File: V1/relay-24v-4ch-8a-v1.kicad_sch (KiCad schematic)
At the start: 22 parts, among them J1 DG141V-2.54-6P, J2 DB142V-5.08-8P, K1 G5Q-1A4-DC24V, K2 G5Q-1A4-DC24V, K3 G5Q-1A4-DC24V, K4 G5Q-1A4-DC24V

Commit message: Prefab checks
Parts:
- D1, D3, D5, D7: value GREEN -> EMERALD; LCSC Part # C72043 -> C2984266; Mfr Everlight -> Everlight Elec; Mfr PN 19-217/GHC-YR1S2/3T -> 19-213/GHC-XS1T1N/5T; Vendor PN C72043 -> C2984266
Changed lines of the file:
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@@
 			)
 		)
-		(property "Value" "GREEN"
+		(property "Value" "EMERALD"
 			(at 162.56 120.65 90)
 			(effects
@@
 			)
 		)
-		(property "Mfr" "Everlight"
+		(property "Mfr" "Everlight Elec"
 			(at 165.1 120.65 0)
 			(effects
@@
 			)
 		)
-		(property "Mfr PN" "19-217/GHC-YR1S2/3T"
+		(property "Mfr PN" "19-213/GHC-XS1T1N/5T"
 			(at 165.1 120.65 0)
 			(effects
@@
 			)
 		)
-		(property "Vendor PN" "C72043"
+		(property "Vendor PN" "C2984266"
 			(at 165.1 120.65 0)
 			(effects
@@
 			)
 		)
-		(property "LCSC Part #" "C72043"
+		(property "LCSC Part #" "C2984266"
 			(at 162.56 123.19 90)
 			(effects
@@
 			)
 		)
-		(property "Value" "GREEN"
+		(property "Value" "EMERALD"
 			(at 74.93 118.11 90)
 			(effects
@@
 			)
 		)
-		(property "Mfr" "Everlight"
+		(property "Mfr" "Everlight Elec"
 			(at 77.47 118.11 0)
 			(effects
@@
 			)
 		)
-		(property "Mfr PN" "19-217/GHC-YR1S2/3T"
+		(property "Mfr PN" "19-213/GHC-XS1T1N/5T"
 			(at 77.47 118.11 0)
 			(effects
@@
 			)
 		)
-		(property "Vendor PN" "C72043"
+		(property "Vendor PN" "C2984266"
 			(at 77.47 118.11 0)
 			(effects
@@
 			)
 		)
-		(property "LCSC Part #" "C72043"
+		(property "LCSC Part #" "C2984266"
 			(at 74.93 120.65 90)
 			(effects
@@
 			)
 		)
-		(property "Value" "GREEN"
+		(property "Value" "EMERALD"
 			(at 74.93 80.01 90)
 			(effects
@@
 			)
 		)
-		(property "Mfr" "Everlight"
+		(property "Mfr" "Everlight Elec"
 			(at 77.47 80.01 0)
 			(effects
@@
 			)
 		)
-		(property "Mfr PN" "19-217/GHC-YR1S2/3T"
+		(property "Mfr PN" "19-213/GHC-XS1T1N/5T"
 			(at 77.47 80.01 0)
 			(effects
@@
 			)
 		)
-		(property "Vendor PN" "C72043"
+		(property "Vendor PN" "C2984266"
 			(at 77.47 80.01 0)
 			(effects
@@
 			)
 		)
-		(property "LCSC Part #" "C72043"
+		(property "LCSC Part #" "C2984266"
 			(at 74.93 82.55 90)
 			(effects
@@
 			)
 		)
-		(property "Value" "GREEN"
+		(property "Value" "EMERALD"
 			(at 162.56 82.55 90)
 			(effects
@@
 			)
 		)
-		(property "Mfr" "Everlight"
+		(property "Mfr" "Everlight Elec"
 			(at 165.1 82.55 0)
 			(effects
@@
 			)
 		)
-		(property "Mfr PN" "19-217/GHC-YR1S2/3T"
+		(property "Mfr PN" "19-213/GHC-XS1T1N/5T"
 			(at 165.1 82.55 0)
 			(effects
@@
 			)
 		)
-		(property "Vendor PN" "C72043"
+		(property "Vendor PN" "C2984266"
 			(at 165.1 82.55 0)
 			(effects
@@
 			)
 		)
-		(property "LCSC Part #" "C72043"
+		(property "LCSC Part #" "C2984266"
 			(at 162.56 85.09 90)
 			(effects

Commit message: Updated footprints
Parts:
- removed J2: DB142V-5.08-8P, Tales:TerminalBlock_Dibo_DB142V-5.08-8P_1x08_P5.08mm_Vertical, symbol Connector_Generic:Conn_01x08
- added J2, J3: Conn_01x04, Tales:TerminalBlock_Dibo_DB142V-5.08-4P_1x04_P5.08mm_Vertical, symbol Connector_Generic:Conn_01x04
- J1: value DG141V-2.54-6P -> DB141V-2.54-6P; LCSC Part # C2898747 -> C2898748; Mfr DIBO -> DORABO; Vendor PN C2898747 -> C2898748
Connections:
- net at K3.2, RV3.2: now also J3.2 (Pin_2)
- net at K3.3, RV3.1: now also J3.1 (Pin_1)
- net at K4.2, RV4.2: now also J3.4 (Pin_4)
- net at K4.3, RV4.1: now also J3.3 (Pin_3)
- net at K1.2, RV1.2: now also J2.2 (Pin_2)
- net at K1.3, RV1.1: now also J2.1 (Pin_1)
- net at K2.3, RV2.1: now also J2.3 (Pin_3)
- net at K2.2, RV2.2: now also J2.4 (Pin_4)

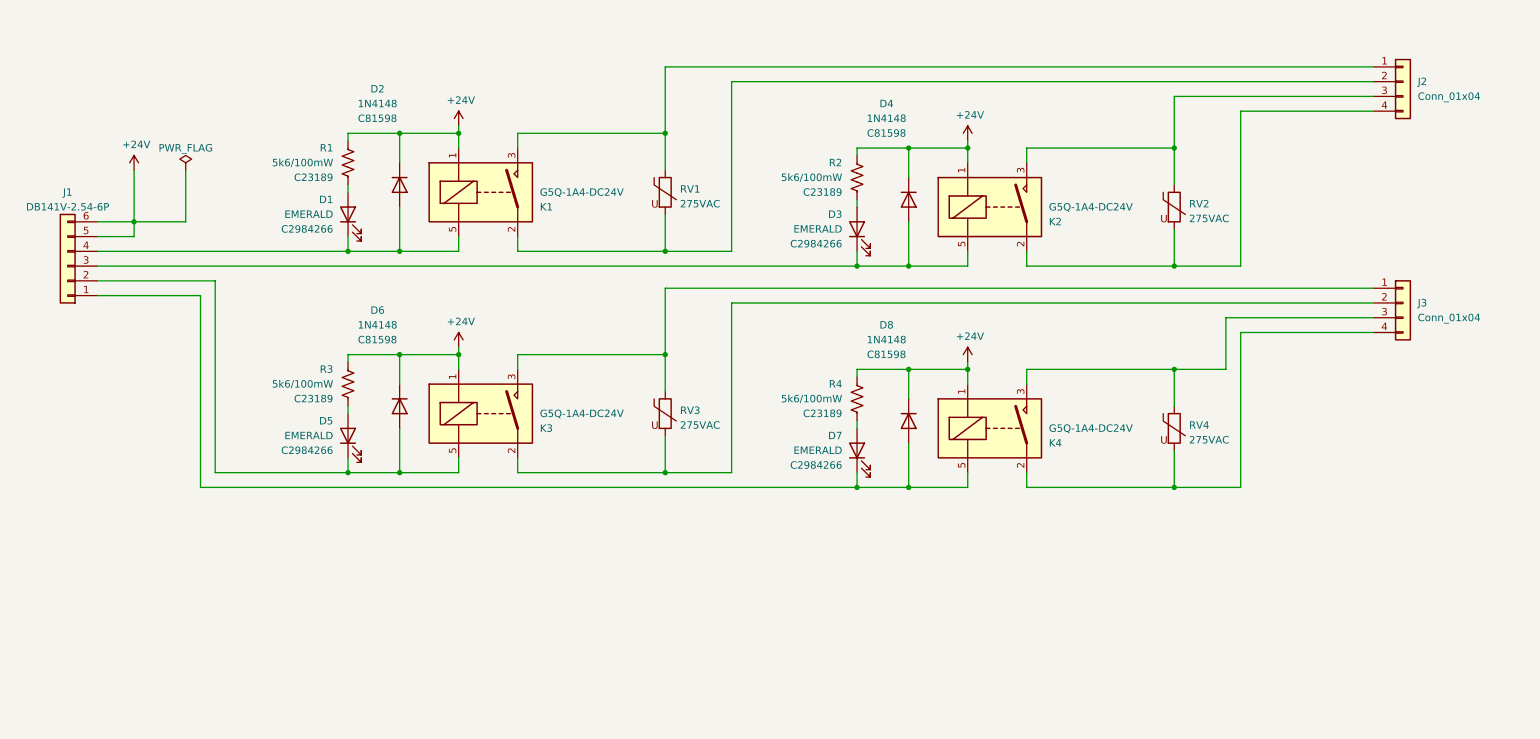
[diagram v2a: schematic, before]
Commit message: Updated connectors
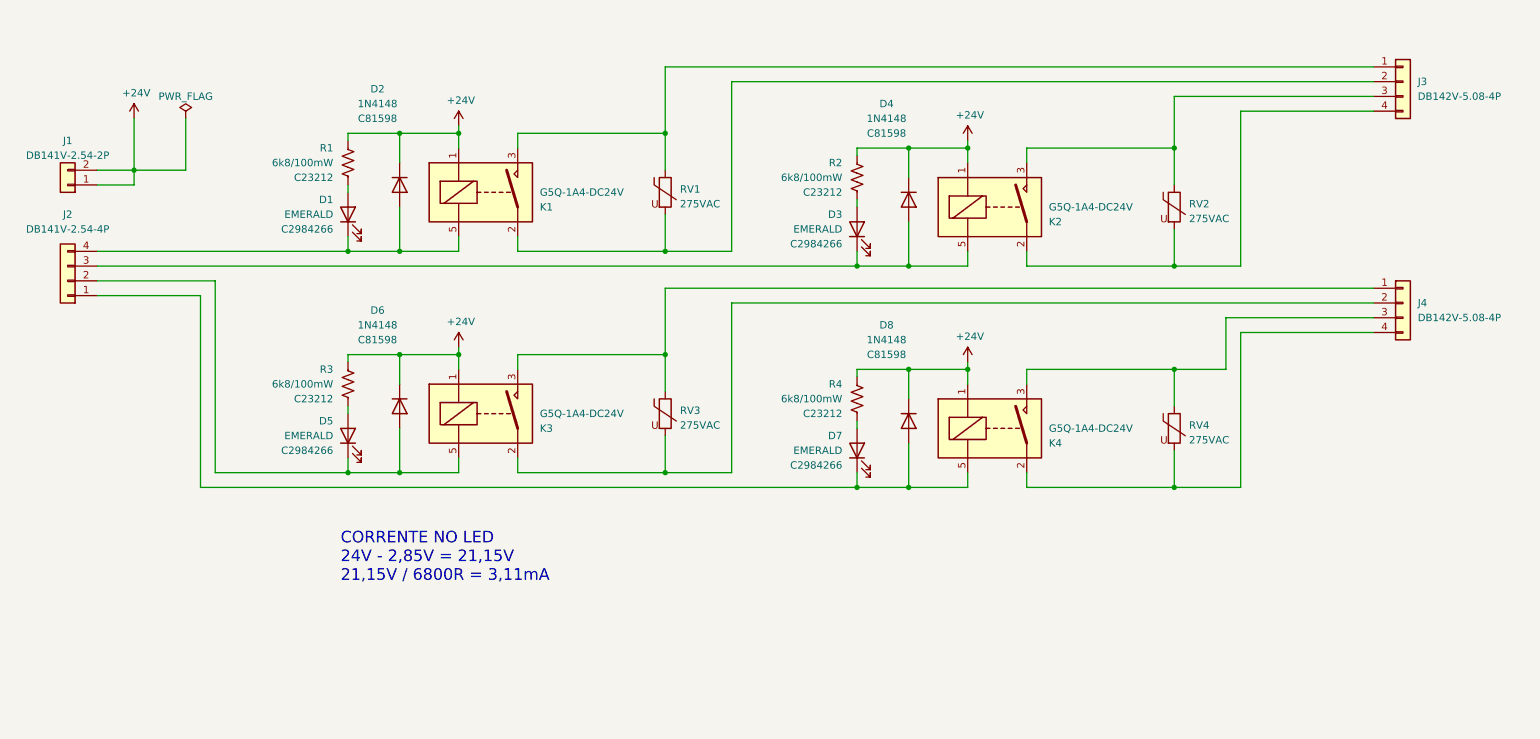
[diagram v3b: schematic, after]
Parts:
- removed J1: DB141V-2.54-6P, Tales:TerminalBlock_Dibo_DB141V-2.54-6P_1x06_P2.54mm_Vertical, symbol Connector_Generic:Conn_01x06
- added J1: DB141V-2.54-2P, Tales:TerminalBlock_Dibo_DB141V-2.54-2P_1x02_P2.54mm_Vertical, symbol Connector_Generic:Conn_01x02
- added J2: DB141V-2.54-4P, Tales:TerminalBlock_Dibo_DB141V-2.54-4P_1x04_P2.54mm_Vertical, symbol Connector_Generic:Conn_01x04
- J3: renamed from J2; value Conn_01x04 -> DB142V-5.08-4P
- J4: renamed from J3; value Conn_01x04 -> DB142V-5.08-4P
- R1, R2, R3, R4: value 5k6/100mW -> 6k8/100mW; LCSC Part # C23189 -> C23212; Mfr PN 0805W8F4701T5E -> 0603WAF6801T5E; Vendor PN C23189 -> C23212
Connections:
- net +24V: now also J1.1 (Pin_1), J1.2 (Pin_2)
- net at D7.1 (K), D8.2 (A), K4.5: now also J2.1 (Pin_1)
- net at D5.1 (K), D6.2 (A), K3.5: now also J2.2 (Pin_2)
- net at D1.1 (K), D2.2 (A), K1.5: now also J2.4 (Pin_4)
- net at D3.1 (K), D4.2 (A), K2.5: now also J2.3 (Pin_3)
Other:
- note added: "CORRENTE NO LED 24V - 2,85V = 21,15V 21,15V / 6800R = 3,11mA"

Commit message: Revising for fabrication
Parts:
- D1, D3, D5, D7: value EMERALD -> WHITE; LCSC Part # C2984266 -> C2290; Mfr Everlight Elec -> Hubei KENTO Elec; Mfr PN 19-213/GHC-XS1T1N/5T -> KT-0603W; Vendor PN C2984266 -> C2290
- R1, R2, R3, R4: value 6k8/100mW -> 10k/100mW; LCSC Part # C23212 -> C25804; Mfr Uniroyal -> UNI-ROYAL(Uniroyal Elec); Mfr PN 0603WAF6801T5E -> 0603WAF1002T5E; Vendor PN C23212 -> C25804
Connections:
- net IN4: now reaches D7.1 (K), D8.2 (A), J2.1 (Pin_1), K4.5
- net LED4: now reaches D7.2 (A), R4.2
- net OUT3LD: now reaches J4.2 (Pin_2), K3.2, RV3.2
- net OUT3PW: now reaches J4.1 (Pin_1), K3.3, RV3.1
- net IN3: now reaches D5.1 (K), D6.2 (A), J2.2 (Pin_2), K3.5
- net IN1: now reaches D1.1 (K), D2.2 (A), J2.4 (Pin_4), K1.5
- net LED1: now reaches D1.2 (A), R1.2
- net IN2: now reaches D3.1 (K), D4.2 (A), J2.3 (Pin_3), K2.5
- net LED3: now reaches D5.2 (A), R3.2
- net OUT4LD: now reaches J4.4 (Pin_4), K4.2, RV4.2
- net OUT4PW: now reaches J4.3 (Pin_3), K4.3, RV4.1
- net OUT1LD: now reaches J3.2 (Pin_2), K1.2, RV1.2
- net OUT1PW: now reaches J3.1 (Pin_1), K1.3, RV1.1
- net OUT2PW: now reaches J3.3 (Pin_3), K2.3, RV2.1
- net OUT2LD: now reaches J3.4 (Pin_4), K2.2, RV2.2
- net LED2: now reaches D3.2 (A), R2.2
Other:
- note added: "CORRENTE NO LED 24V - 2,85V = 21,15V 21,15V / 10K = 2,11mA"
- note removed: "CORRENTE NO LED 24V - 2,85V = 21,15V 21,15V / 6800R = 3,11mA"
- moved on the sheet: D1, D2, D3, D4, D5, D6, D7, D8, J4, K1, K2, K3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

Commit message: Review before fabrication
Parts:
- J1: LCSC Part # (none) -> C2898744; Mfr (none) -> DORABO; Mfr PN (none) -> DB141V-2.54-2P-GN; Vendor PN (none) -> C2898744
- J2: LCSC Part # (none) -> C2898746; Mfr (none) -> DORABO; Mfr PN (none) -> DB141V-2.54-4P-GN; Vendor PN (none) -> C2898746
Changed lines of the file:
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@@
 			)
 		)
+		(property "LCSC Part #" "C2898744"
+			(at 29.21 74.93 0)
+			(effects
+				(font
+					(size 1.27 1.27)
+				)
+				(hide yes)
+			)
+		)
+		(property "Mfr" "DORABO"
+			(at 29.21 74.93 0)
+			(effects
+				(font
+					(size 1.27 1.27)
+				)
+				(hide yes)
+			)
+		)
+		(property "Mfr PN" "DB141V-2.54-2P-GN"
+			(at 29.21 74.93 0)
+			(effects
+				(font
+					(size 1.27 1.27)
+				)
+				(hide yes)
+			)
+		)
+		(property "Package" "~"
+			(at 29.21 74.93 0)
+			(effects
+				(font
+					(size 1.27 1.27)
+				)
+				(hide yes)
+			)
+		)
+		(property "Vendor PN" "C2898744"
+			(at 29.21 74.93 0)
+			(effects
+				(font
+					(size 1.27 1.27)
+				)
+				(hide yes)
+			)
+		)
 		(pin "2"
 		)
@@
 		(dnp no)
 		(property "Reference" "K3"
-			(at 113.03 135.89 0)
+			(at 113.03 130.81 0)
 			(effects
 				(font
@@
 		)
 		(property "LCSC Part #" "C2931104"
-			(at 104.14 133.35 0)
+			(at 118.11 135.89 0)
 			(effects
 				(font
 					(size 1.27 1.27)
 				)
-				(hide yes)
 			)
 		)
@@
 			)
 		)
+		(property "LCSC Part #" "C2898746"
+			(at 29.21 91.44 0)
+			(effects
+				(font
+					(size 1.27 1.27)
+				)
+				(hide yes)
+			)
+		)
+		(property "Mfr" "DORABO"
+			(at 29.21 91.44 0)
+			(effects
+				(font
+					(size 1.27 1.27)
+				)
+				(hide yes)
+			)
+		)
+		(property "Mfr PN" "DB141V-2.54-4P-GN"
+			(at 29.21 91.44 0)
+			(effects
+				(font
+					(size 1.27 1.27)
+				)
+				(hide yes)
+			)
+		)
+		(property "Package" "~"
+			(at 29.21 91.44 0)
+			(effects
+				(font
+					(size 1.27 1.27)
+				)
+				(hide yes)
+			)
+		)
+		(property "Vendor PN" "C2898746"
+			(at 29.21 91.44 0)
+			(effects
+				(font
+					(size 1.27 1.27)
+				)
+				(hide yes)
+			)
+		)
 		(pin "4"
 		)
@@
 		(dnp no)
 		(property "Reference" "K4"
-			(at 204.47 139.7 0)
+			(at 204.47 134.62 0)
 			(effects
 				(font
@@
 		)
 		(property "LCSC Part #" "C2931104"
-			(at 195.58 137.16 0)
+			(at 209.55 139.7 0)
 			(effects
 				(font
 					(size 1.27 1.27)
 				)
-				(hide yes)
 			)
 		)
@@
 		(dnp no)
 		(property "Reference" "K1"
-			(at 113.03 73.66 0)
+			(at 113.03 68.58 0)
 			(effects
 				(font
@@
 		)
 		(property "LCSC Part #" "C2931104"
-			(at 104.14 71.12 0)
+			(at 118.11 73.66 0)
 			(effects
 				(font
 					(size 1.27 1.27)
 				)
-				(hide yes)
 			)
 		)
@@
 		(dnp no)
 		(property "Reference" "K2"
-			(at 204.47 77.47 0)
+			(at 204.47 72.39 0)
 			(effects
 				(font
@@
 		)
 		(property "LCSC Part #" "C2931104"
-			(at 195.58 74.93 0)
+			(at 209.55 77.47 0)
 			(effects
 				(font
 					(size 1.27 1.27)
 				)
-				(hide yes)
 			)
 		)

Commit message: Revising before manufacturing.
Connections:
- net OUT1PW renamed OUT1LN
- net OUT2PW renamed OUT2LN
- net OUT3PW renamed OUT3LN
- net OUT4PW renamed OUT4LN
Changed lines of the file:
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@@
 		)
 	)
-	(label "OUT3PW"
+	(label "OUT3LN"
 		(at 245.11 116.84 0)
 		(effects
@@
 		)
 	)
-	(label "OUT4PW"
+	(label "OUT4LN"
 		(at 245.11 121.92 0)
 		(effects
@@
 		)
 	)
-	(label "OUT1PW"
+	(label "OUT1LN"
 		(at 245.11 54.61 0)
 		(effects
@@
 		)
 	)
-	(label "OUT2PW"
+	(label "OUT2LN"
 		(at 245.11 59.69 0)
 		(effects
